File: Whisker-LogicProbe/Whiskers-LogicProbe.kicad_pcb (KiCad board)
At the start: 2 copper layers, 31.2 x 25 mm, 34 parts, among them J1 Conn_01x10_Male, J10 Conn_01x04_Male, J11 Conn_01x04_Male, J9 USB_B_Micro, U1 SN65LVDS(T)348, U2 MIC5504-3.3YM5

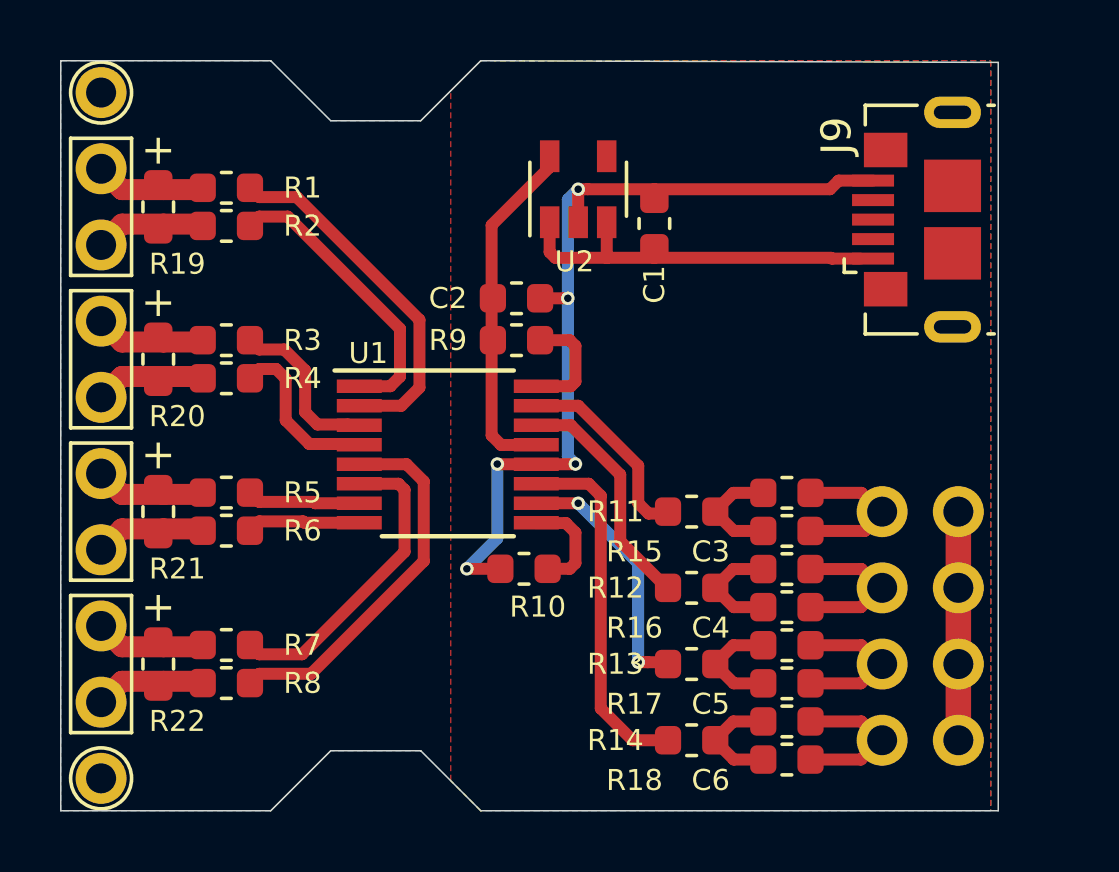
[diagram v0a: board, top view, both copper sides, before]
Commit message: Updated to use the proper LVDS receiver chip (560Mb/s one)
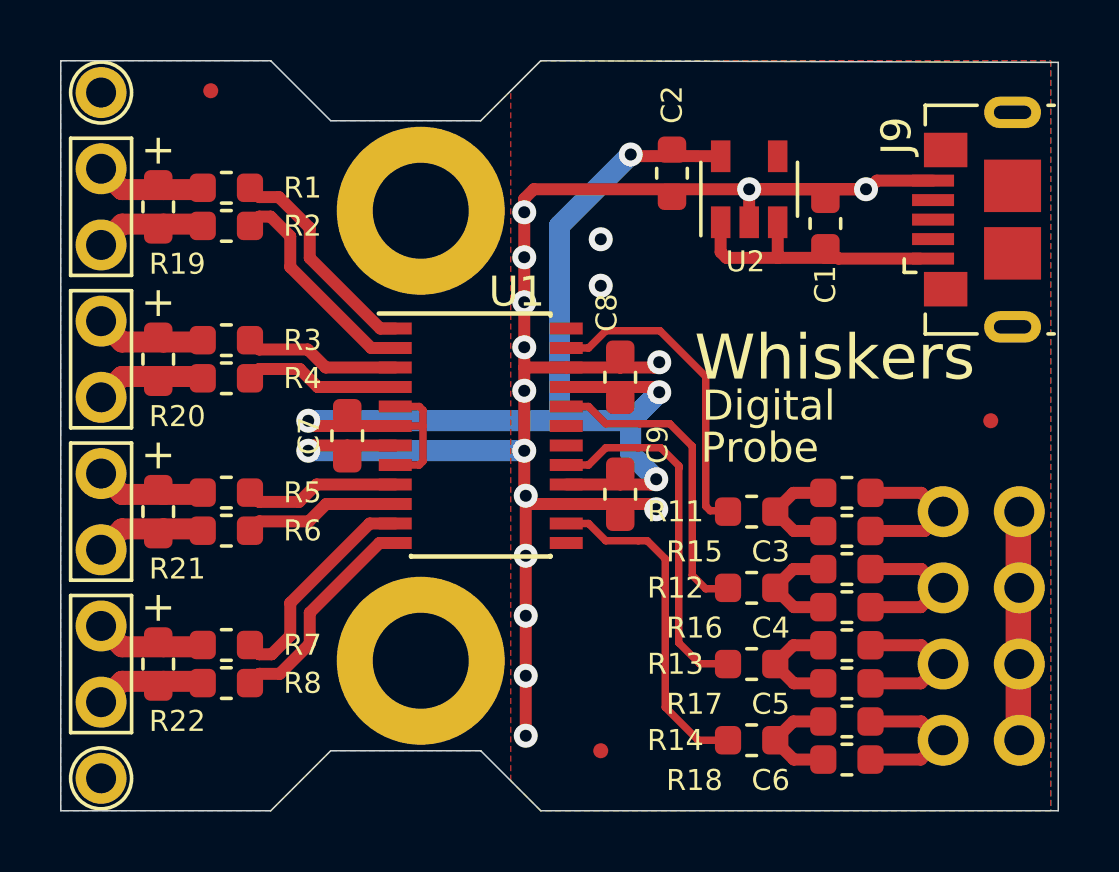
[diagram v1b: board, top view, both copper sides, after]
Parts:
- removed R10, R9: 250, Resistor_SMD:R_0603_1608Metric
- added C7: 0.1uF, Capacitor_SMD:C_0603_1608Metric, F.Cu at (101.5, 110.5)
- added C8: 0.1uF, Capacitor_SMD:C_0603_1608Metric, F.Cu at (110.7, 108.5)
- added C9: 0.1uF, Capacitor_SMD:C_0603_1608Metric, F.Cu at (110.7, 112.5)
- added FID1: Fiducial, Fiducial:Fiducial_0.5mm_Mask1mm, F.Cu at (97.0, 99.0)
- added FID2: Fiducial, Fiducial:Fiducial_0.5mm_Mask1mm, F.Cu at (110.0, 121.0)
- added FID3: Fiducial, Fiducial:Fiducial_0.5mm_Mask1mm, F.Cu at (123.0, 110.0)
- added H1: MountingHole_Pad, MountingHole:MountingHole_3.2mm_M3_DIN965_Pad, F.Cu at (104.0, 103.0)
- added H2: MountingHole_Pad, MountingHole:MountingHole_3.2mm_M3_DIN965_Pad, F.Cu at (104.0, 118.0)
- U1: value SN65LVDS(T)348 -> SN65LVDS(T)352; footprint Package_SO:TSSOP-16_4.4x5mm_P0.65mm -> Package_SO:TSSOP-24_4.4x7.8mm_P0.65mm
- moved C2 6.65 mm to (112.4, 101.8), turned to 90 degrees
- moved C1 5.70 mm to (117.5, 103.4)
- moved U2 5.70 mm to (114.9, 102.3)
- moved J10 2.03 mm to (121.4, 113.0)
- moved J11 2.03 mm to (124.0, 120.7)
- moved C3 2.00 mm to (118.2, 113.7)
- moved C4 2.00 mm to (118.2, 116.2)
- moved C5 2.00 mm to (118.2, 118.8)
- moved C6 2.00 mm to (118.2, 121.3)
- moved J9 2.00 mm to (122.5, 103.3)
- moved R11 2.00 mm to (115.0, 113.0)
- moved R12 2.00 mm to (115.0, 115.6)
- moved R13 2.00 mm to (115.0, 118.1)
- moved R14 2.00 mm to (115.0, 120.7)
- moved R15 2.00 mm to (118.2, 112.4)
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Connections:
- U1 pad 1: /IN1- -> /IN1+
- U1 pad 10: /OUT3 -> /IN3-
- U1 pad 11: /OUT4 -> /IN4+
- U1 pad 12: GNDREF -> /IN4-
- U1 pad 13: +3V3 -> Net-(U1-Pad13)
- U1 pad 14: /OUT2 -> /OUT4
- U1 pad 15: /OUT1 -> GNDREF
- U1 pad 16: Net-(R9-Pad2) -> +3V3
- U1 pad 2: /IN1+ -> /IN1-
- U1 pad 5: /IN4- -> +3V3
- U1 pad 6: /IN4+ -> +3V3
- U1 pad 7: /IN3+ -> GNDREF
- U1 pad 8: /IN3- -> +3V3
- U1 pad 9: Net-(R10-Pad1) -> /IN3+
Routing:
- net +3V3: track 11.8 -> 42.8 mm, vias 0 -> 4
- net GNDREF: track 37.1 -> 65.4 mm, vias 5 -> 18
- net /IN4-: track 12.5 -> 7.38 mm
- net /IN1+: track 12.0 -> 7.37 mm
- net /OUT1: track 6.64 -> 10.7 mm
- net Net-(R9-Pad2): track 3.78 -> 0.00 mm
- net +5V: track 13.0 -> 9.37 mm
- net /OUT3: track 8.60 -> 12.1 mm, vias 2 -> 0
- net Net-(R10-Pad1): track 3.49 -> 0.00 mm
- net /IN4+: track 10.4 -> 7.42 mm
- net /OUT2: track 7.99 -> 10.4 mm
- net /IN1-: track 9.76 -> 7.39 mm
- net /IN3-: track 3.79 -> 5.21 mm
- net /IN3+: track 3.79 -> 5.21 mm
- net /OUT4: track 12.1 -> 11.4 mm
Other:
- board size 31.2 x 25 mm -> 33.2 x 25 mm
- board text added: "Design by LoialOtter"
- board text added: "Digital"
- board text added: "Probe"
- board text added: "Whiskers"
